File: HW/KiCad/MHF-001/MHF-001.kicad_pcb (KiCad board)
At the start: 2 copper layers, 252.9 x 100.2 mm, 219 parts, among them J1 DE15_Socket_HighDensity_Mount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, J10 I2C, J11 POWER, J2 Mini-DIN-6, J3 Conn_Coaxial, J4 Conn_02x32_Odd_Even, J5 USB_B_Micro, J6 02x32, J7 SPI, J8 AVR-ISP-6, J9 Serial, M3 CY7C109D-10ZXI, M5 CY7C109D-10ZXI, Q1 BC107, U1 ATMEGA2560-16AU, U10 74HC245, U11 74HC245, U12 74HC245, U13 CH340G, U14 AMS1117-5.0, U15 AMS1117-3.3, U2 74HC14, U3 74LS08, U4 74HC165, U6 74AHC373PW, U7 74HC595, U8 74HC595, U9 74HC157, Y1 16 MHz, Y2 12 MHz

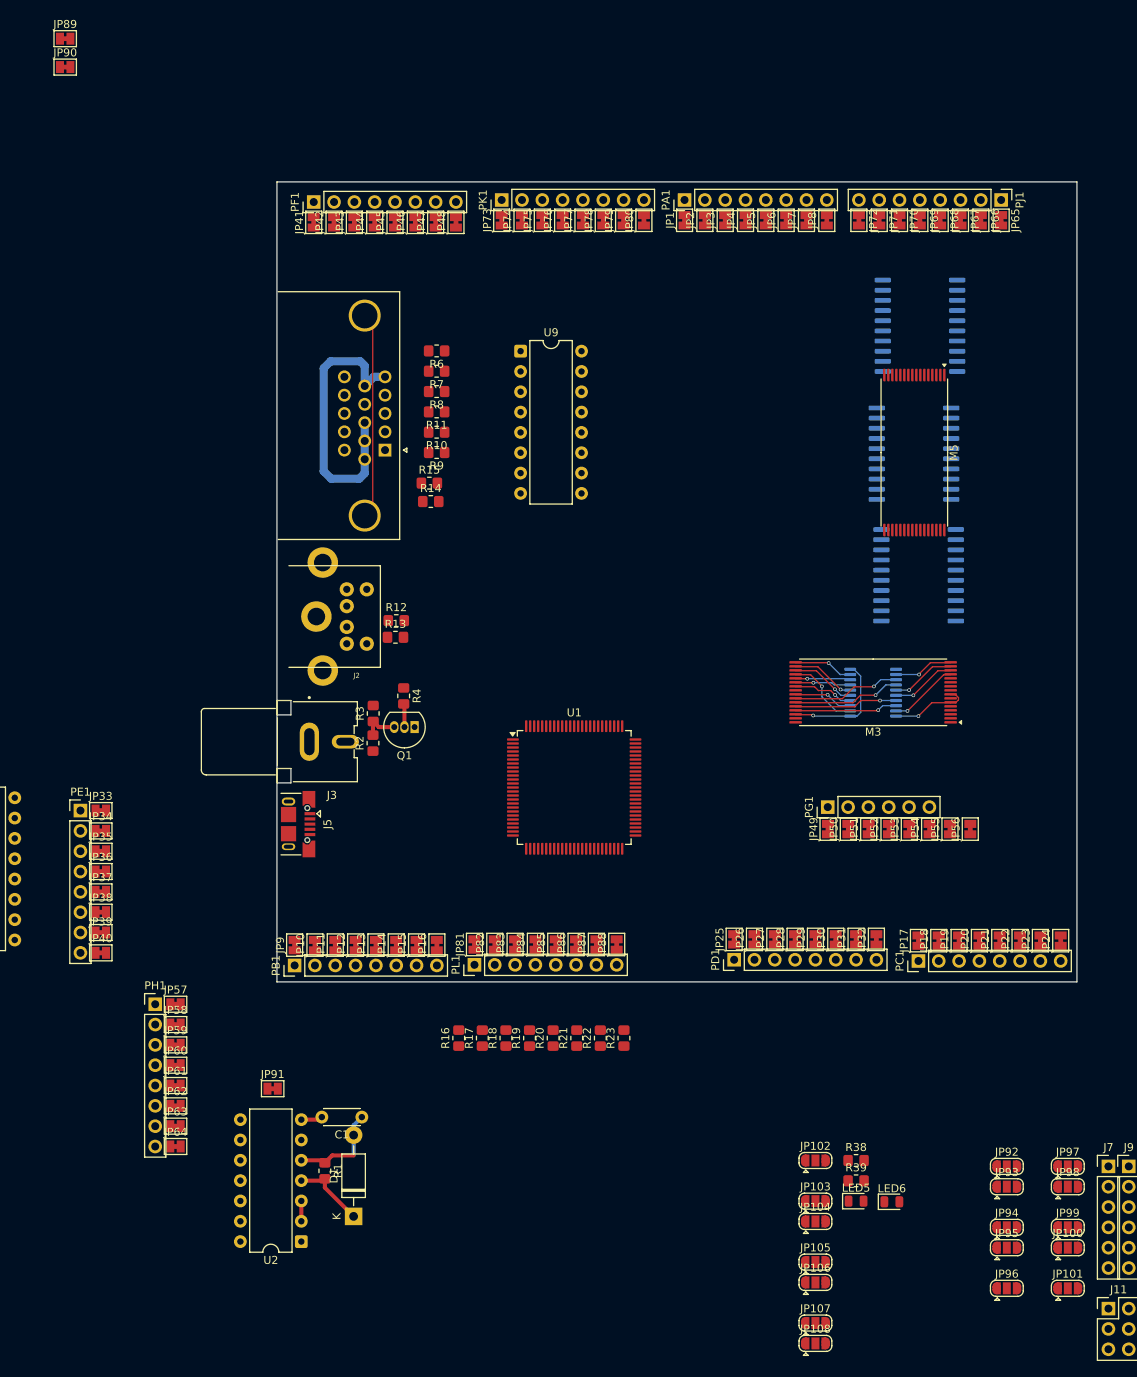
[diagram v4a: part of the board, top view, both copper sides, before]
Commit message: saved lot of pins by removing unnecessery/redundant signals
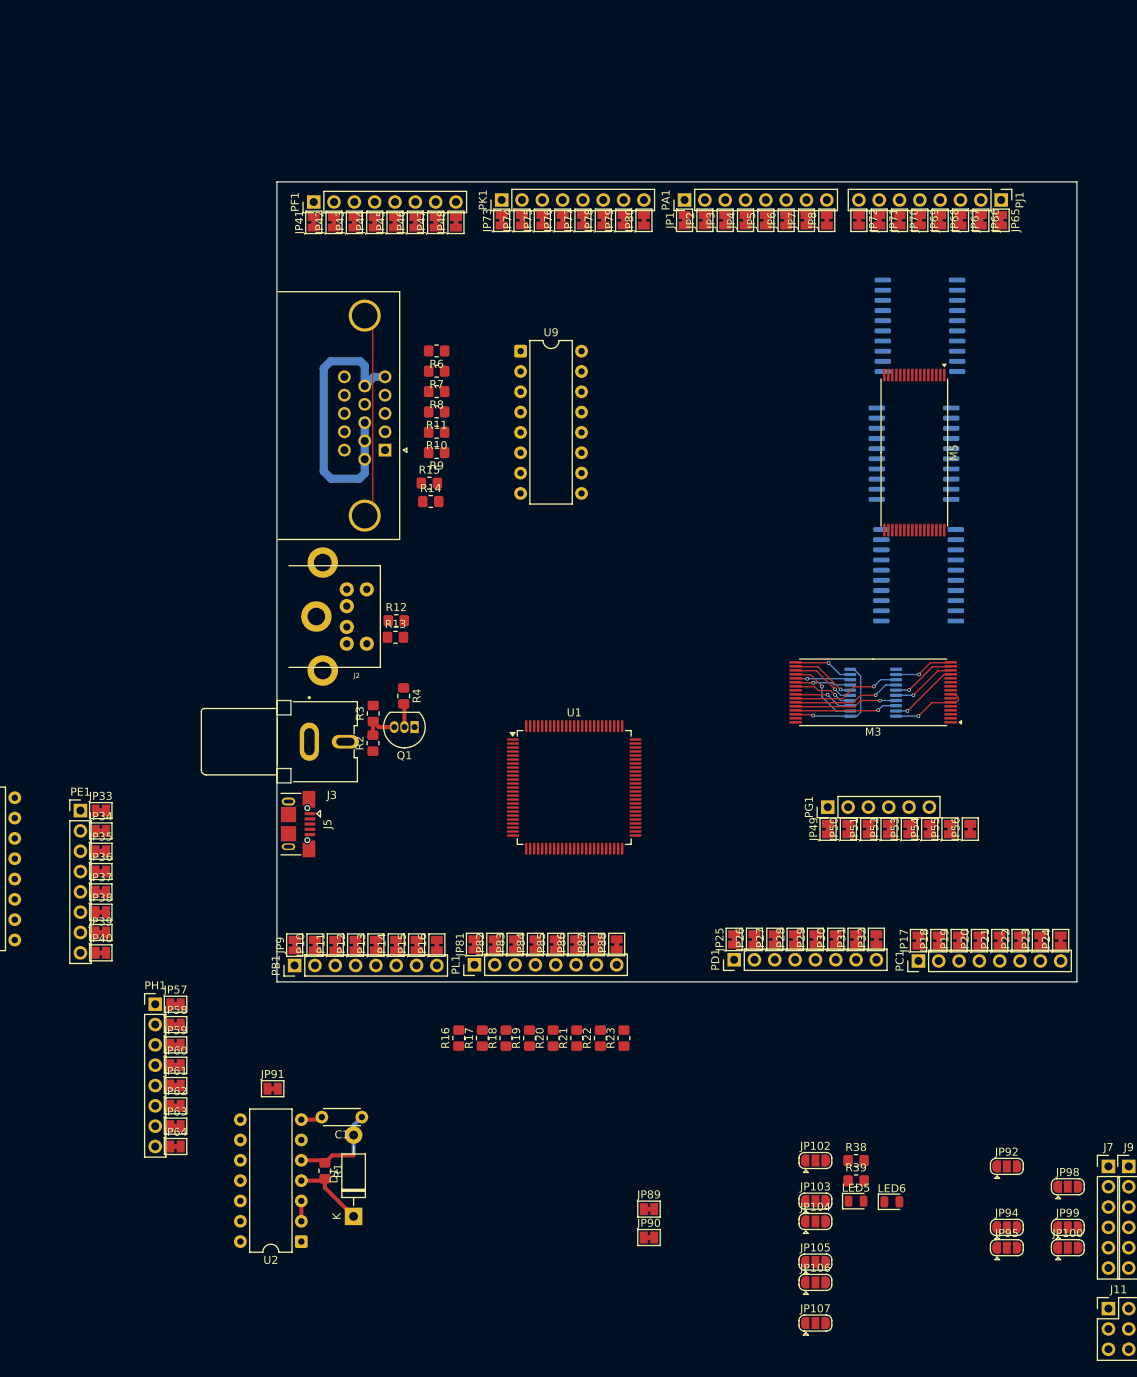
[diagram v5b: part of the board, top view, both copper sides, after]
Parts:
- removed JP101, JP108, JP93, JP96, JP97: SolderJumper_3_Open, Jumper:SolderJumper-3_P1.3mm_Open_RoundedPad1.0x1.5mm
- moved JP89 163.5 mm to (74.6, 147.6)
- moved JP90 163.5 mm to (74.6, 151.1)
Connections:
- J4 pad 29: A_BUS -> A_HALT
- J4 pad 30: B_BUS -> B_HALT
- J4 pad 31: A_HALT -> A_READ
- J4 pad 32: B_HALT -> B_READ
- J4 pad 33: A_READ -> A_SHARE_DIRTY
- J4 pad 34: B_READ -> B_SHARE_DIRTY
- J4 pad 35: A_WRITE -> A_SHARE_GRANTED
- J4 pad 36: B_WRITE -> B_SHARE_GRANTED
- J4 pad 37: A_SHARE_BUSY -> A_SHARE_REQUEST
- J4 pad 38: B_SHARE_BUSY -> B_SHARE_REQUEST
- J4 pad 39: A_SHARE_DIRTY -> A_S_ENABLE
- J4 pad 40: B_SHARE_DIRTY -> B_S_ENABLE
- J4 pad 41: A_SHARE_GRANTED -> A_S_READ
- J4 pad 42: B_SHARE_GRANTED -> B_S_READ
- J4 pad 43: A_SHARE_REQUEST -> A_S_WRITE
- J4 pad 44: B_SHARE_REQUEST -> B_S_WRITE
- J4 pad 45: A_SHARE_WANTED -> A_G_D_DIR
- J4 pad 46: B_SHARE_WANTED -> B_G_D_DIR
- J4 pad 47: A_S_ENABLE -> A_G_A_DIR
- J4 pad 48: B_S_ENABLE -> B_G_A_DIR
- J4 pad 49: A_S_READ -> A_G_ENABLE
- J4 pad 50: B_S_READ -> B_G_ENABLE
- J4 pad 51: A_S_WRITE -> unconnected-(J4-Pin_51-Pad51)
- J4 pad 52: B_S_WRITE -> unconnected-(J4-Pin_52-Pad52)
- J4 pad 53: A_G_D_DIR -> unconnected-(J4-Pin_53-Pad53)
- J4 pad 54: B_G_D_DIR -> unconnected-(J4-Pin_54-Pad54)
- J4 pad 55: A_G_D_OE -> unconnected-(J4-Pin_55-Pad55)
- J4 pad 56: B_G_D_OE -> unconnected-(J4-Pin_56-Pad56)
- J4 pad 57: A_G_A_DIR -> unconnected-(J4-Pin_57-Pad57)
- J4 pad 58: B_G_A_DIR -> unconnected-(J4-Pin_58-Pad58)
- J4 pad 59: A_G_A_OE -> unconnected-(J4-Pin_59-Pad59)
- J4 pad 60: B_G_A_OE -> unconnected-(J4-Pin_60-Pad60)
- J6 pad 29: A_BUS -> A_HALT
- J6 pad 30: B_BUS -> B_HALT
- J6 pad 31: A_HALT -> A_READ
- J6 pad 32: B_HALT -> B_READ
- J6 pad 33: A_READ -> A_SHARE_DIRTY
- J6 pad 34: B_READ -> B_SHARE_DIRTY
- J6 pad 35: A_WRITE -> A_SHARE_GRANTED
- J6 pad 36: B_WRITE -> B_SHARE_GRANTED
- J6 pad 37: A_SHARE_BUSY -> A_SHARE_REQUEST
- J6 pad 38: B_SHARE_BUSY -> B_SHARE_REQUEST
- J6 pad 39: A_SHARE_DIRTY -> A_S_ENABLE
- J6 pad 40: B_SHARE_DIRTY -> B_S_ENABLE
- J6 pad 41: A_SHARE_GRANTED -> A_S_READ
- J6 pad 42: B_SHARE_GRANTED -> B_S_READ
- J6 pad 43: A_SHARE_REQUEST -> A_S_WRITE
- J6 pad 44: B_SHARE_REQUEST -> B_S_WRITE
- J6 pad 45: A_SHARE_WANTED -> A_G_D_DIR
- J6 pad 46: B_SHARE_WANTED -> B_G_D_DIR
- J6 pad 47: A_S_ENABLE -> A_G_A_DIR
- J6 pad 48: B_S_ENABLE -> B_G_A_DIR
- J6 pad 49: A_S_READ -> A_G_ENABLE
- J6 pad 50: B_S_READ -> B_G_ENABLE
- J6 pad 51: A_S_WRITE -> unconnected-(J6-Pin_51-Pad51)
- J6 pad 52: B_S_WRITE -> unconnected-(J6-Pin_52-Pad52)
- J6 pad 53: A_G_D_DIR -> unconnected-(J6-Pin_53-Pad53)
- J6 pad 54: B_G_D_DIR -> unconnected-(J6-Pin_54-Pad54)
- J6 pad 55: A_G_D_OE -> unconnected-(J6-Pin_55-Pad55)
- J6 pad 56: B_G_D_OE -> unconnected-(J6-Pin_56-Pad56)
- J6 pad 57: A_G_A_DIR -> unconnected-(J6-Pin_57-Pad57)
- J6 pad 58: B_G_A_DIR -> unconnected-(J6-Pin_58-Pad58)
- J6 pad 59: A_G_A_OE -> unconnected-(J6-Pin_59-Pad59)
- J6 pad 60: B_G_A_OE -> unconnected-(J6-Pin_60-Pad60)
- JP106 pad 1: A_G_D_OE -> A_G_ENABLE
- JP106 pad 2: G_D_OE -> G_ENABLE
- JP106 pad 3: B_G_D_OE -> B_G_ENABLE
- JP27 pad 2: /X_READ -> /X_HALT
- JP28 pad 2: /X_WRITE -> /X_READ
- JP29 pad 2: /X_SHARE_BUSY -> /X_SHARE_GRANTED
- JP30 pad 2: /X_SHARE_DIRTY -> /X_SHARE_REQUEST
- JP31 pad 2: /X_SHARE_GRANTED -> /X_SHARE_DIRTY
- JP32 pad 2: /X_SHARE_REQUEST -> unconnected-(JP32-B-Pad2)
- JP38 pad 2: /X_SHARE_WANTED -> unconnected-(JP38-B-Pad2)
- JP53 pad 2: /X_HALT -> unconnected-(JP53-B-Pad2)
- JP54 pad 2: /X_BUS -> unconnected-(JP54-B-Pad2)
- U10 pad 19: G_D_OE -> G_ENABLE
- U11 pad 19: G_A_OE -> G_ENABLE
- U12 pad 19: G_A_OE -> G_ENABLE

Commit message: +NetJoint
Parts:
- added J12: Reset, Connector_Wire:SolderWire-0.5sqmm_1x01_D0.9mm_OD2.1mm, F.Cu at (207.3, 61.5)
- added J13: AREF, Connector_Wire:SolderWire-0.5sqmm_1x01_D0.9mm_OD2.1mm, F.Cu at (207.3, 65.7)
- added J14: XTAL2, Connector_Wire:SolderWire-0.5sqmm_1x01_D0.9mm_OD2.1mm, F.Cu at (207.3, 69.9)
- added J15: XTAL1, Connector_Wire:SolderWire-0.5sqmm_1x01_D0.9mm_OD2.1mm, F.Cu at (207.3, 74.1)
- added J16: AVCC, Connector_Wire:SolderWire-0.5sqmm_1x01_D0.9mm_OD2.1mm, F.Cu at (207.3, 78.3)
- added JP93: SolderJumper_2_Bridged, Jumper:SolderJumper-2_P1.3mm_Bridged_Pad1.0x1.5mm, F.Cu at (233.8, 54.1)
- added N1: ~, Gilhad:NetJoint, F.Cu at (229.5, 53.6)
- added N2: ~, Gilhad:NetJoint, F.Cu at (229.5, 56.2)
- added N3: ~, Gilhad:NetJoint, F.Cu at (229.5, 58.8)
- added N4: ~, Gilhad:NetJoint, F.Cu at (229.5, 61.4)
- R32, R33: footprint Resistor_SMD:R_0603_1608Metric_Pad0.98x0.95mm_HandSolder -> Resistor_SMD:R_0805_2012Metric_Pad1.20x1.40mm_HandSolder
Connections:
- J10 pad 1: SDA -> SCL
- J10 pad 2: SCL -> SDA
- J10 pad 3: GND -> +5V
- J10 pad 4: +5V -> GND
- JP14 pad 2: Shared_Address_A16 -> /X16
- JP27 pad 2: /X_HALT -> unconnected-(JP27-B-Pad2)
- JP28 pad 2: /X_READ -> SIGNAL_RCA
- JP32 pad 2: unconnected-(JP32-B-Pad2) -> /X_READ
- JP38 pad 2: unconnected-(JP38-B-Pad2) -> /X_HALT
- JP85 pad 2: SYNC_RCA -> VGA data 4
- JP92 pad 2: Shared_Address_A16 -> /X16
- R5 pad 1: Bb -> SIGNAL_RCA
- U1 pad 100: +5V -> Net-(J16-Pin_1)
- U3 pad 1: Bb -> SIGNAL_RCA
- U3 pad 2: VGA data 3 -> ~{SUPRESS}
- U4 pad 3: SYNC_RCA -> VGA data 4

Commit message: cleaning
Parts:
- removed JP1, JP10, JP11, JP12, JP13, JP14, JP15, JP16, JP2, JP3, JP4, JP5, JP6, JP7, JP8, JP9: SolderJumper_2_Bridged, Jumper:SolderJumper-2_P1.3mm_Bridged_Pad1.0x1.5mm
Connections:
- PA1 pad 1: PA0 -> XAD0
- PA1 pad 2: PA1 -> XAD1
- PA1 pad 3: PA2 -> XAD2
- PA1 pad 4: PA3 -> XAD3
- PA1 pad 5: PA4 -> XAD4
- PA1 pad 6: PA5 -> XAD5
- PA1 pad 7: PA6 -> XAD6
- PA1 pad 8: PA7 -> XAD7
- PB1 pad 1: PB0 -> SS
- PB1 pad 2: PB1 -> SCK
- PB1 pad 3: PB2 -> MOSI
- PB1 pad 4: PB3 -> MISO
- PB1 pad 5: PB4 -> PS2-OE
- PB1 pad 6: PB5 -> /X16
- PB1 pad 7: PB6 -> HSyncVGA
- PB1 pad 8: PB7 -> VGA Latch
- U1 pad 19: PB0 -> SS
- U1 pad 20: PB1 -> SCK
- U1 pad 21: PB2 -> MOSI
- U1 pad 22: PB3 -> MISO
- U1 pad 23: PB4 -> PS2-OE
- U1 pad 24: PB5 -> /X16
- U1 pad 25: PB6 -> HSyncVGA
- U1 pad 26: PB7 -> VGA Latch
- U1 pad 71: PA7 -> XAD7
- U1 pad 72: PA6 -> XAD6
- U1 pad 73: PA5 -> XAD5
- U1 pad 74: PA4 -> XAD4
- U1 pad 75: PA3 -> XAD3
- U1 pad 76: PA2 -> XAD2
- U1 pad 77: PA1 -> XAD1
- U1 pad 78: PA0 -> XAD0

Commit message: added some connectors
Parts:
- removed JP17, JP18, JP19, JP20, JP21, JP22, JP23, JP24, JP25, JP26, JP27, JP28, JP29, JP30, JP31, JP32, JP33, JP34, JP35, JP36, JP37, JP38, JP39, JP40, JP41, JP42, JP43, JP44, JP45, JP46, JP47, JP48, JP49, JP50, JP51, JP52, JP53, JP54, JP57, JP58, JP59, JP60, JP61, JP62, JP63, JP64, JP65, JP66, JP67, JP68, JP69, JP70, JP71, JP72, JP73, JP74, JP75, JP76, JP77, JP78, JP79, JP80, JP81, JP82, JP83, JP84, JP85, JP86, JP87, JP88: SolderJumper_2_Bridged, Jumper:SolderJumper-2_P1.3mm_Bridged_Pad1.0x1.5mm
- removed N1, N2: ~, Gilhad:NetJoint
- added J17: SDcard, Connector_PinHeader_2.54mm:PinHeader_1x06_P2.54mm_Vertical, F.Cu at (238.8, 147.3)
- added J18: RTC1, Connector_PinHeader_2.54mm:PinHeader_1x04_P2.54mm_Vertical, F.Cu at (204.4, 138.9)
- added J19: RTC2, Connector_PinHeader_2.54mm:PinHeader_1x06_P2.54mm_Vertical, F.Cu at (209.0, 138.9)
- added J20: SDcardpins, Connector_PinHeader_2.54mm:PinHeader_1x04_P2.54mm_Vertical, F.Cu at (233.7, 147.3)
- added J21: 5V, Connector_PinHeader_2.54mm:PinHeader_1x02_P2.54mm_Vertical, F.Cu at (157.5, 160.0)
- added J22: 3.3V, Connector_PinHeader_2.54mm:PinHeader_1x02_P2.54mm_Vertical, F.Cu at (162.6, 160.0)
- added J23: VIN 12V, Connector_BarrelJack:BarrelJack_Horizontal, F.Cu at (170.2, 149.9)
- added JP1: SolderJumper_2_Bridged, Jumper:SolderJumper-2_P1.3mm_Bridged_Pad1.0x1.5mm, F.Cu at (231.1, 139.7)
- added JP2: SolderJumper_2_Bridged, Jumper:SolderJumper-2_P1.3mm_Bridged_Pad1.0x1.5mm, F.Cu at (231.1, 142.2)
- added JP3: SolderJumper_2_Bridged, Jumper:SolderJumper-2_P1.3mm_Bridged_Pad1.0x1.5mm, F.Cu at (231.1, 144.8)
- added JP4: SolderJumper_2_Bridged, Jumper:SolderJumper-2_P1.3mm_Bridged_Pad1.0x1.5mm, F.Cu at (231.1, 147.3)
- added R40: 1k, Resistor_SMD:R_0603_1608Metric_Pad0.98x0.95mm_HandSolder, F.Cu at (204.3, 150.0)
- J11: value POWER -> 5V
- turned F1 to 180 degrees
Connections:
- net PD2 renamed Net-(PD1-Pin_3)
- net PG4 renamed Net-(PG1-Pin_5)
- net PG5 renamed Net-(PG1-Pin_6)
- J10 pad 1: SCL -> GND
- J10 pad 2: SDA -> +5V
- J10 pad 3: +5V -> SDA
- J10 pad 4: GND -> SCL
- J11 pad 1: VIN -> +5V
- J11 pad 3: VIN -> +5V
- J11 pad 5: VIN -> +5V
- J7 pad 1: MISO -> SS
- J7 pad 2: MOSI -> SCK
- J7 pad 3: SCK -> MOSI
- J7 pad 4: SS -> MISO
- J7 pad 5: GND -> +5V
- J7 pad 6: +5V -> GND
- JP100 pad 2: /X_SHARE_REQUEST -> X_SHARE_REQUEST
- JP92 pad 2: /X16 -> X16
- JP94 pad 2: /X_HALT -> X_HALT
- JP95 pad 2: /X_READ -> X_READ
- JP98 pad 2: /X_SHARE_DIRTY -> X_SHARE_DIRTY
- JP99 pad 2: /X_SHARE_GRANTED -> X_SHARE_GRANTED
- LED6 pad 1: GND -> SCL
- M5 pad 10: Shared_Address_A16 -> X16
- M5 pad 21: Mega_6309_data0 -> Shared_data_D0
- M5 pad 22: Mega_6309_data1 -> Shared_data_D1
- M5 pad 23: Mega_6309_data2 -> Shared_data_D2
- M5 pad 25: Mega_6309_data3 -> Shared_data_D3
- M5 pad 26: Mega_6309_data4 -> Shared_data_D4
- M5 pad 27: Mega_6309_data5 -> Shared_data_D5
- M5 pad 28: Mega_6309_data6 -> Shared_data_D6
- M5 pad 29: Mega_6309_data7 -> Shared_data_D7
- M5 pad 30: GND -> S_ENABLE
- M5 pad 6: S_ENABLE -> +5V
- PB1 pad 6: /X16 -> X16
- PC1 pad 1: PC0 -> XAA0
- PC1 pad 2: PC1 -> XAA1
- PC1 pad 3: PC2 -> XAA2
- PC1 pad 4: PC3 -> XAA3
- PC1 pad 5: PC4 -> XAA4
- PC1 pad 6: PC5 -> XAA5
- PC1 pad 7: PC6 -> XAA6
- PC1 pad 8: PC7 -> XAA7
- PD1 pad 1: PD0 -> SCL
- PD1 pad 2: PD1 -> SDA
- PD1 pad 4: PD3 -> SIGNAL_RCA
- PD1 pad 5: PD4 -> X_SHARE_GRANTED
- PD1 pad 6: PD5 -> X_SHARE_REQUEST
- PD1 pad 7: PD6 -> X_SHARE_DIRTY
- PD1 pad 8: PD7 -> X_READ
- PE1 pad 1: PE0 -> TX
- PE1 pad 2: PE1 -> RX
- PE1 pad 3: PE2 -> CTS
- PE1 pad 4: PE3 -> RTS
- PE1 pad 5: PE4 -> VSyncVGA
- PE1 pad 6: PE5 -> X_HALT
- PE1 pad 7: PE6 -> Inside
- PE1 pad 8: PE7 -> 16MHz
- PF1 pad 1: PF0 -> Shared_data_D0
- PF1 pad 2: PF1 -> Shared_data_D1
- PF1 pad 3: PF2 -> Shared_data_D2
- PF1 pad 4: PF3 -> Shared_data_D3
- PF1 pad 5: PF4 -> Shared_data_D4
- PF1 pad 6: PF5 -> Shared_data_D5
- PF1 pad 7: PF6 -> Shared_data_D6
- PF1 pad 8: PF7 -> Shared_data_D7
- PG1 pad 1: PG0 -> WE
- PG1 pad 2: PG1 -> RD
- PG1 pad 3: PG2 -> ALE
- PG1 pad 4: PG3 -> XAA16
- PH1 pad 1: PH0 -> Ib
- PH1 pad 2: PH1 -> Bb
- PH1 pad 3: PH2 -> Gb
- PH1 pad 4: PH3 -> Rb
- PH1 pad 5: PH4 -> If
- PH1 pad 6: PH5 -> Bf
- PH1 pad 7: PH6 -> Gf
- PH1 pad 8: PH7 -> Rf
- PJ1 pad 1: PJ0 -> Shared_Address_A0
- PJ1 pad 2: PJ1 -> Shared_Address_A1
- PJ1 pad 3: PJ2 -> Shared_Address_A2
- PJ1 pad 4: PJ3 -> Shared_Address_A3
- PJ1 pad 5: PJ4 -> Shared_Address_A4
- PJ1 pad 6: PJ5 -> Shared_Address_A5
- PJ1 pad 7: PJ6 -> Shared_Address_A6
- PJ1 pad 8: PJ7 -> Shared_Address_A7
- PK1 pad 1: PK0 -> Shared_Address_A8
- PK1 pad 2: PK1 -> Shared_Address_A9
- PK1 pad 3: PK2 -> Shared_Address_A10
- PK1 pad 4: PK3 -> Shared_Address_A11
- PK1 pad 5: PK4 -> Shared_Address_A12
- PK1 pad 6: PK5 -> Shared_Address_A13
- PK1 pad 7: PK6 -> Shared_Address_A14
- PK1 pad 8: PK7 -> Shared_Address_A15
- PL1 pad 1: PL0 -> VGA data 0
- PL1 pad 2: PL1 -> VGA data 1
- PL1 pad 3: PL2 -> VGA data 2
- PL1 pad 4: PL3 -> VGA data 3
- PL1 pad 5: PL4 -> VGA data 4
- PL1 pad 6: PL5 -> VGA data 5
- PL1 pad 7: PL6 -> VGA data 6
- PL1 pad 8: PL7 -> VGA data 7
- R32 pad 2: PD1 -> SDA
- R33 pad 2: PD0 -> SCL
- R38 pad 2: CTS -> RTS
- R39 pad 2: RTS -> +5V
- U1 pad 12: PH0 -> Ib
- U1 pad 13: PH1 -> Bb
- U1 pad 14: PH2 -> Gb
- U1 pad 15: PH3 -> Rb
- U1 pad 16: PH4 -> If
- U1 pad 17: PH5 -> Bf
- U1 pad 18: PH6 -> Gf
- U1 pad 2: PE0 -> TX
- U1 pad 24: /X16 -> X16
- U1 pad 27: PH7 -> Rf
- U1 pad 28: PG3 -> XAA16
- U1 pad 3: PE1 -> RX
- U1 pad 35: PL0 -> VGA data 0
- U1 pad 36: PL1 -> VGA data 1
- U1 pad 37: PL2 -> VGA data 2
- U1 pad 38: PL3 -> VGA data 3
- U1 pad 39: PL4 -> VGA data 4
- U1 pad 4: PE2 -> CTS
- U1 pad 40: PL5 -> VGA data 5
- U1 pad 41: PL6 -> VGA data 6
- U1 pad 42: PL7 -> VGA data 7
- U1 pad 43: PD0 -> SCL
- U1 pad 44: PD1 -> SDA
- U1 pad 46: PD3 -> SIGNAL_RCA
- U1 pad 47: PD4 -> X_SHARE_GRANTED
- U1 pad 48: PD5 -> X_SHARE_REQUEST
- U1 pad 49: PD6 -> X_SHARE_DIRTY
- U1 pad 5: PE3 -> RTS
- U1 pad 50: PD7 -> X_READ
- U1 pad 51: PG0 -> WE
- U1 pad 52: PG1 -> RD
- U1 pad 53: PC0 -> XAA0
- U1 pad 54: PC1 -> XAA1
- U1 pad 55: PC2 -> XAA2
- U1 pad 56: PC3 -> XAA3
- U1 pad 57: PC4 -> XAA4
- U1 pad 58: PC5 -> XAA5
- U1 pad 59: PC6 -> XAA6
- U1 pad 6: PE4 -> VSyncVGA
- U1 pad 60: PC7 -> XAA7
- U1 pad 63: PJ0 -> Shared_Address_A0
- U1 pad 64: PJ1 -> Shared_Address_A1
- U1 pad 65: PJ2 -> Shared_Address_A2
- U1 pad 66: PJ3 -> Shared_Address_A3
- U1 pad 67: PJ4 -> Shared_Address_A4
- U1 pad 68: PJ5 -> Shared_Address_A5
- U1 pad 69: PJ6 -> Shared_Address_A6
- U1 pad 7: PE5 -> X_HALT
- U1 pad 70: PG2 -> ALE
- U1 pad 79: PJ7 -> Shared_Address_A7
- U1 pad 8: PE6 -> Inside
- U1 pad 82: PK7 -> Shared_Address_A15
- U1 pad 83: PK6 -> Shared_Address_A14
- U1 pad 84: PK5 -> Shared_Address_A13
- U1 pad 85: PK4 -> Shared_Address_A12
- U1 pad 86: PK3 -> Shared_Address_A11
- U1 pad 87: PK2 -> Shared_Address_A10
- U1 pad 88: PK1 -> Shared_Address_A9
- U1 pad 89: PK0 -> Shared_Address_A8
- U1 pad 9: PE7 -> 16MHz
- U1 pad 90: PF7 -> Shared_data_D7
- U1 pad 91: PF6 -> Shared_data_D6
- U1 pad 92: PF5 -> Shared_data_D5
- U1 pad 93: PF4 -> Shared_data_D4
- U1 pad 94: PF3 -> Shared_data_D3
- U1 pad 95: PF2 -> Shared_data_D2
- U1 pad 96: PF1 -> Shared_data_D1
- U1 pad 97: PF0 -> Shared_data_D0
- U10 pad 2: Mega_6309_data0 -> Shared_data_D0
- U10 pad 3: Mega_6309_data1 -> Shared_data_D1
- U10 pad 4: Mega_6309_data2 -> Shared_data_D2
- U10 pad 5: Mega_6309_data3 -> Shared_data_D3
- U10 pad 6: Mega_6309_data4 -> Shared_data_D4
- U10 pad 7: Mega_6309_data5 -> Shared_data_D5
- U10 pad 8: Mega_6309_data6 -> Shared_data_D6
- U10 pad 9: Mega_6309_data7 -> Shared_data_D7
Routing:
- net Net-(J17-Pin_4): track 0.00 -> 6.97 mm
- net Net-(J17-Pin_3): track 0.00 -> 6.97 mm
- net Net-(J17-Pin_2): track 0.00 -> 6.97 mm
- net Net-(J17-Pin_1): track 0.00 -> 6.97 mm
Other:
- board text added: "SDcard"
